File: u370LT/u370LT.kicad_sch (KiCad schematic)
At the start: 0 parts

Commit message: Updated northbridge more
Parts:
- added U1: ~, Library:BGA-676_26x26_35.0x35.0mm, symbol Library:VT82C694X
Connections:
- new net: U1.A1 (GND), U1.A14 (GND), U1.A26 (GND), U1.AA19 (GND), U1.AA21 (GND), U1.AA6 (GND), U1.AA8 (GND), U1.AB12 (GND), U1.AB15 (GND), U1.AB24 (GND), U1.AB25 (GND), U1.AC4 (GND), U1.AD18 (GND), U1.AD22 (GND), U1.AD9 (GND), U1.AE23 (GND), U1.AF1 (GND), U1.AF13 (GND), U1.AF26 (GND), U1.C18 (GND), U1.C22 (GND), U1.C5 (GND), U1.C9 (GND), U1.E12 (GND), U1.E15 (GND), U1.E24 (GND), U1.E3 (GND), U1.F19 (GND), U1.F21 (GND), U1.F6 (GND), U1.F8 (GND), U1.H21 (GND), U1.H6 (GND), U1.J24 (GND), U1.J3 (GND), U1.K1 (GND), U1.K7 (GND), U1.L12 (GND), U1.L15 (GND), U1.M11 (GND), U1.M13 (GND), U1.M14 (GND), U1.M16 (GND), U1.N12 (GND), U1.N13 (GND), U1.N14 (GND), U1.N15 (GND), U1.N24 (GND), U1.N7 (GND), U1.P12 (GND), U1.P13 (GND), U1.P14 (GND), U1.P15 (GND), U1.P22 (GND), U1.P26 (GND), U1.P3 (GND), U1.P7 (GND), U1.R11 (GND), U1.R13 (GND), U1.R14 (GND), U1.R16 (GND), U1.R22 (GND), U1.T12 (GND), U1.T15 (GND), U1.U6 (GND), U1.V24 (GND), U1.Y3 (GND), U1.Y6 (GND), U1.Y7 (GND), U1.Y8 (GND)
- new net: U1.AA18 (VCC), U1.AA20 (VCC), U1.AA9 (VCC), U1.AE26 (VCC), U1.AF14 (VCC), U1.B1 (VCC), U1.C2 (VCC), U1.F18 (VCC), U1.F20 (VCC), U1.F7 (VCC), U1.F9 (VCC), U1.G21 (VCC), U1.G6 (VCC), U1.J21 (VCC), U1.J6 (VCC), U1.L11 (VCC), U1.L13 (VCC), U1.L14 (VCC), U1.L16 (VCC), U1.M12 (VCC), U1.M15 (VCC), U1.N11 (VCC), U1.N16 (VCC), U1.N26 (VCC), U1.P11 (VCC), U1.P16 (VCC), U1.R12 (VCC), U1.R15 (VCC), U1.T11 (VCC), U1.T13 (VCC), U1.T14 (VCC), U1.T16 (VCC), U1.V21 (VCC)
- new net: U1.AA3 (VCCQ), U1.AA7 (VCCQ), U1.L6 (VCCQ), U1.L7 (VCCQ), U1.R3 (VCCQ), U1.R6 (VCCQ), U1.R7 (VCCQ)
- new net: U1.AD4 (VCCQQ), U1.W6 (VCCQ)
- new net: U1.L4 (ST0), U1.M4 (ST2)
- new net: U1.M21 (GNDA), U1.M22 (GNDA), U1.U7 (GNDA), U1.W21 (GNDA)
- new net: U1.N21 (VCCA), U1.N22 (VCCA), U1.V6 (VCCA), U1.Y21 (VCCA)

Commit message: NB fixed up, SB started
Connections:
- net at U1.E16 (GTLREF): now also U1.M23 (GTLREF)
- net at U1.F17 (VTT): now also U1.M24 (VTT)
- net at U1.L4 (ST0): no longer U1.M4 (ST2)
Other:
- moved on the sheet: U1
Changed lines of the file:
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@@
 		(pin "U24"
+		)
+		(pin "AF24"
 		)
 		(instances

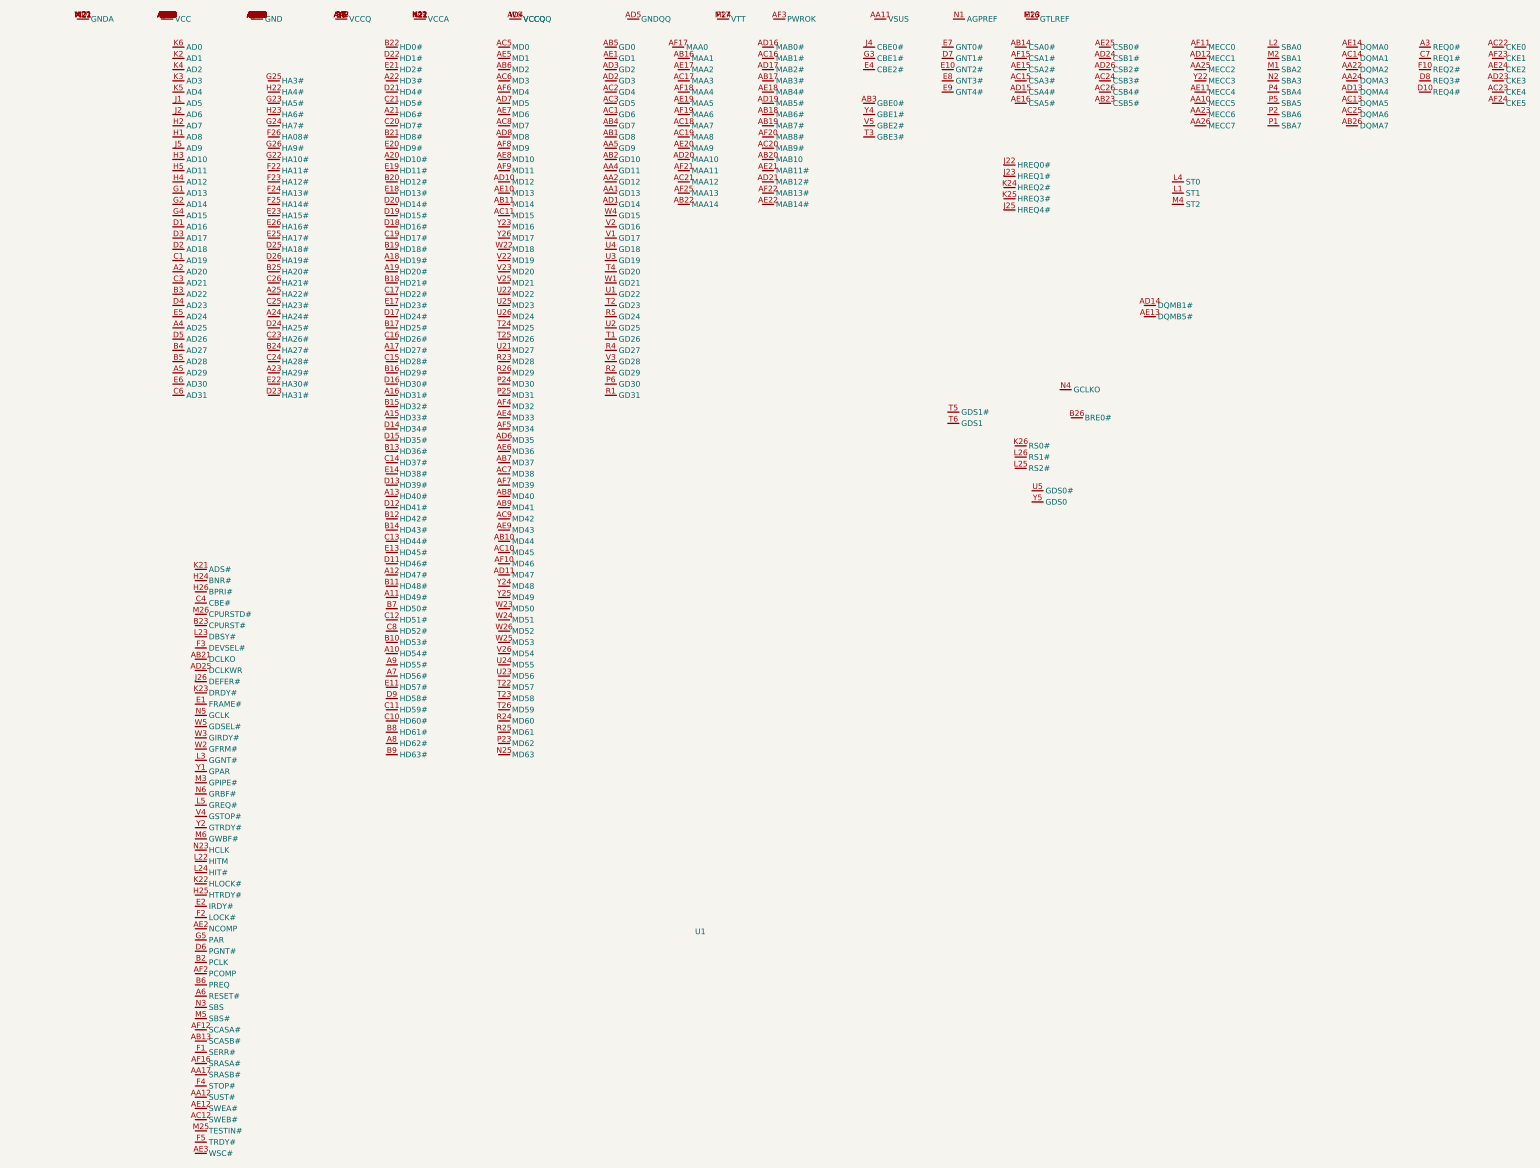
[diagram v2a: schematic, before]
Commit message: Got NB/SB initially placed
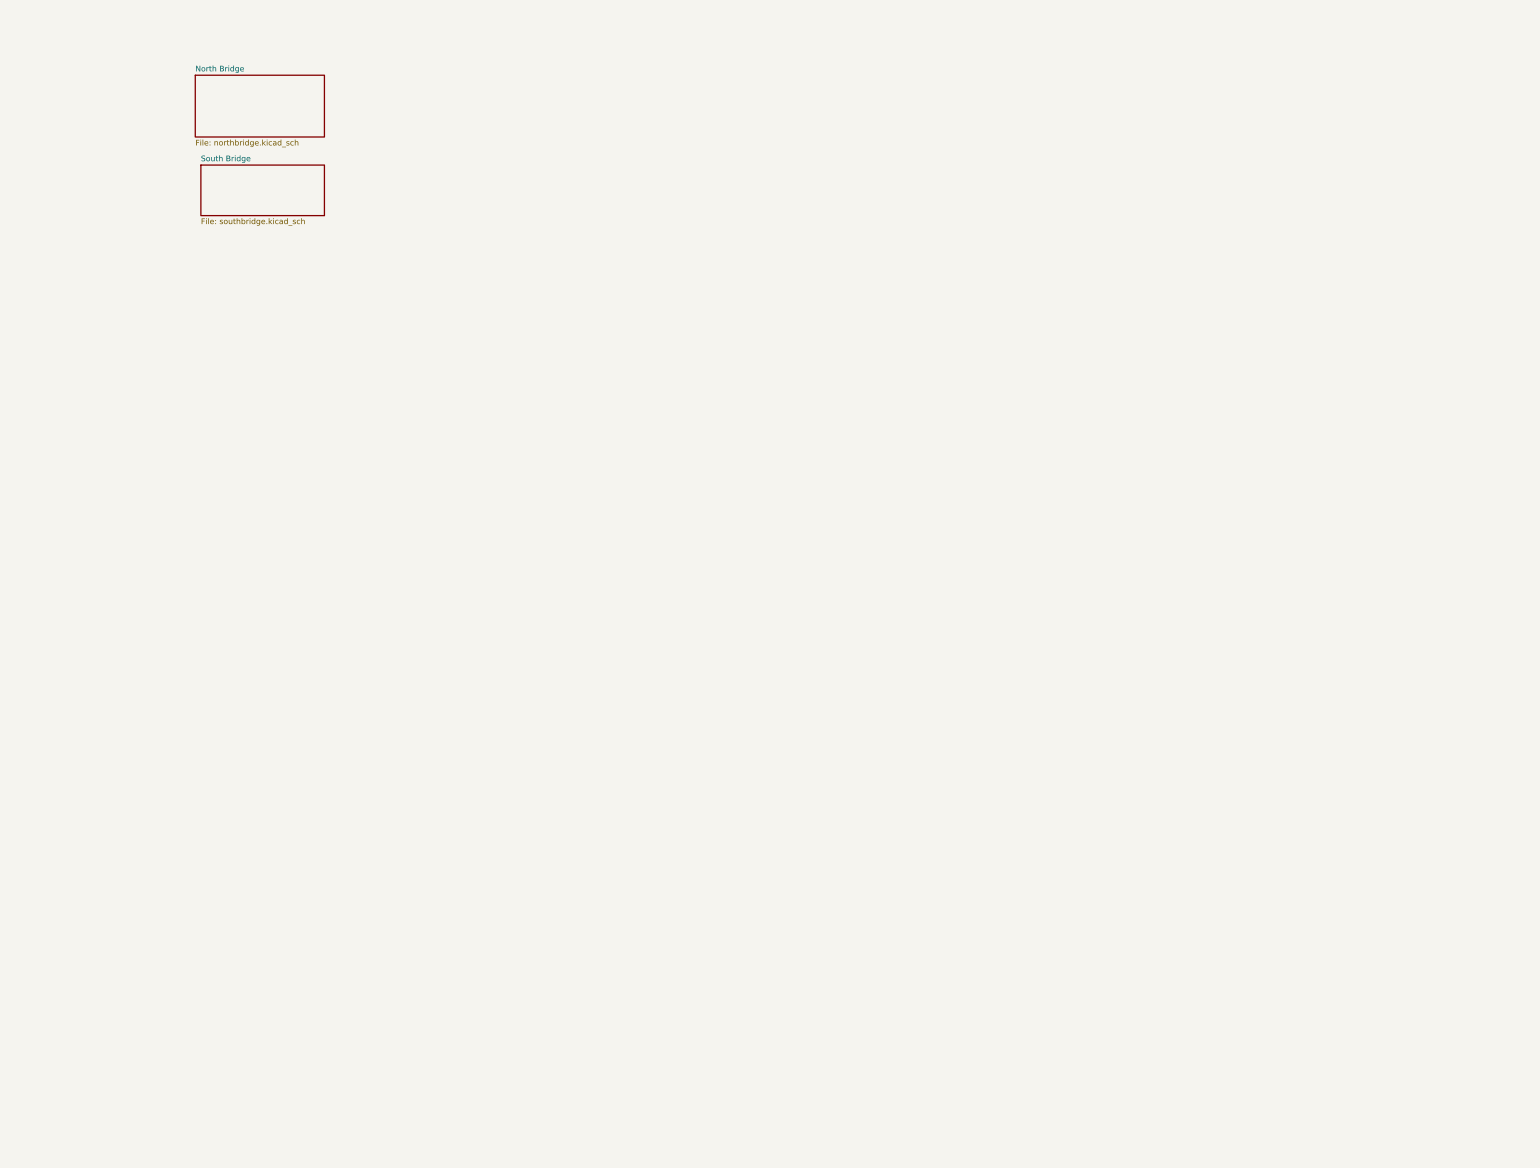
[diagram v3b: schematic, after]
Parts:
- removed U1: ~, Library:BGA-676_26x26_35.0x35.0mm, symbol Library:VT82C694X
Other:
- added sheet North Bridge (northbridge.kicad_sch)
- added sheet South Bridge (southbridge.kicad_sch)
